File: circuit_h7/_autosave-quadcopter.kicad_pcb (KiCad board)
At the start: 4 copper layers, 37.5 x 37.5 mm, 128 parts, among them J1 Conn_01x01_Female, J10 Conn_01x01_Female, J11 Conn_01x04_Male, J13 Conn_01x01_Female, J14 Conn_01x01_Female, J15 Conn_01x01_Female, J16 Conn_01x01_Female, J17 Conn_01x01_Female, J18 USB_C_Receptacle_USB2.0, J19 Conn_01x08_Male, J2 Conn_01x01_Female, J20 Conn_01x01_Female, J21 Conn_01x01_Female, J22 Conn_01x01_Female, J23 Conn_01x01_Female, J24 Conn_01x01_Female, J25 Conn_01x01_Female, J26 Conn_01x01_Female, J27 Conn_01x01_Female, J28 Conn_01x01_Female, J29 Conn_01x01_Female, J3 Conn_01x01_Female, J30 Conn_01x01_Female, J31 Conn_01x01_Female, J32 Conn_01x01_Female, J33 Conn_01x01_Female, J34 Conn_01x01_Female, J35 Conn_01x01_Female, J36 Conn_01x01_Female, J37 Conn_01x01_Female, J4 Conn_01x01_Female, J40 Conn_01x01_Female, J41 Conn_01x01_Female, J42 Conn_01x01_Female, J43 Conn_01x01_Female, J44 Conn_01x01_Female, J45 Conn_01x01_Female, J47 Conn_01x01_Female, J48 Conn_01x01_Female, J49 Conn_01x01_Female, J5 Conn_Coaxial, J50 Conn_01x01_Female, J6 Conn_01x06_Male, J7 Conn_01x01_Female, J8 Conn_01x01_Female, J9 Conn_01x01_Female, SW1 SW_DIP_x01, U1 STM32H723VGH6, U10 ESP8285, U12 TPS5430DDA, U2 ICM-42605, U3 DPS310, U4 3V3, U6 2450FM07D0034T, U7 W25Q80DVUXIE TR (16M), U8 SX1281, Y1 16M, Y2 52Mhz, 12pF, Y3 40M

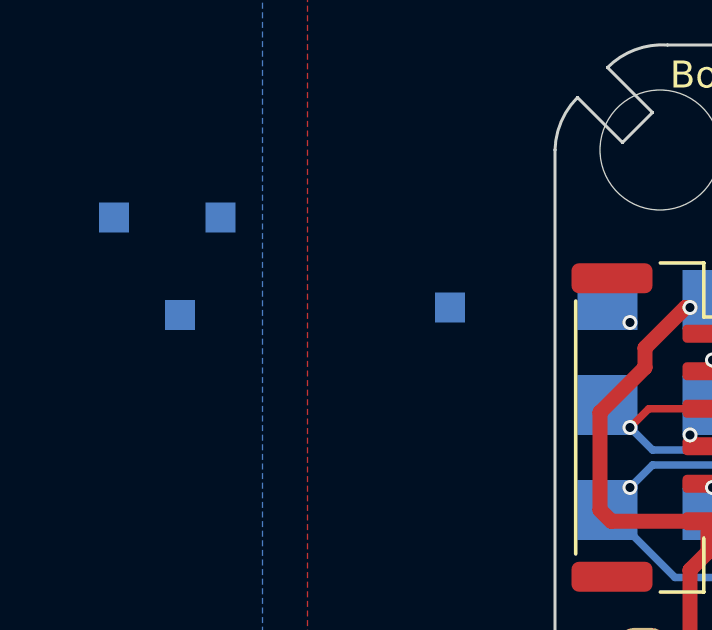
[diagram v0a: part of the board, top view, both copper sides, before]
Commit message: More work on H7 board. Removed ctrl mix from firmware
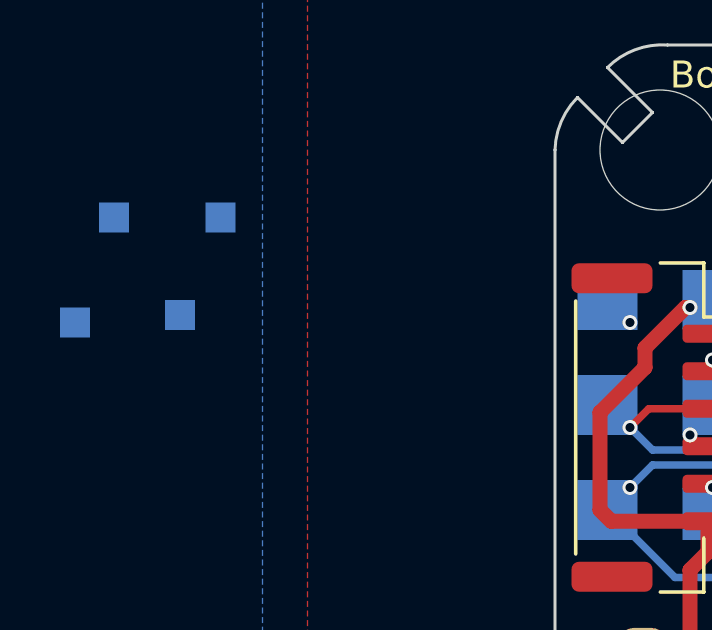
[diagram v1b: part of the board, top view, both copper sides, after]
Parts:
- moved J27 12.5 mm to (102.2, 78.0)
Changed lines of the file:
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@@
   )
   (footprint "TestPoint:TestPoint_Pad_1.0x1.0mm" (layer "B.Cu")
-    (at 114.75 77.5 180)
+    (at 102.25 78 180)
     (descr "SMD rectangular pad as test Point, square 1.0mm side length")
     (tags "test point SMD pad rectangle square")

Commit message: More work on H7 board
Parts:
- removed C42: 150p, Capacitor_SMD:C_0402_1005Metric
- removed C43: 100n, Capacitor_SMD:C_0402_1005Metric
- removed C44: 1.5n, Capacitor_SMD:C_0402_1005Metric
- removed C45, C46: 10u, Capacitor_SMD:C_0805_2012Metric
- removed R17: 300, Resistor_SMD:R_0402_1005Metric
- removed R19: 10k, Resistor_SMD:R_0402_1005Metric
- added C14: 22uF 25v, Capacitor_SMD:C_0805_2012Metric, F.Cu at (132.2, 99.5)
- added C15: 22n, Capacitor_SMD:C_0402_1005Metric, F.Cu at (128.0, 97.2)
- added C20: 100uF 6.3V, Capacitor_SMD:C_1206_3216Metric, F.Cu at (136.0, 94.0)
- added L2: 10u 2A, Inductor_SMD:L_Taiyo-Yuden_MD-4040, F.Cu at (131.2, 95.5)
- added R7: 10k, Resistor_SMD:R_0402_1005Metric, F.Cu at (150.5, 97.8)
- added R8: 100k, Resistor_SMD:R_0402_1005Metric, F.Cu at (124.8, 99.5)
- added U5: MT2492 600kHz 16v 2A, Package_TO_SOT_SMD:SOT-23-6, F.Cu at (129.0, 99.5)
- R10: value 3.3K -> 1.4k
- R11: value 300 -> 13k; footprint Resistor_SMD:R_0402_1005Metric -> Resistor_SMD:R_0603_1608Metric
- U12: value TPS5430DDA -> TPS5430DDA 3A 36v
- moved J27 43.9 mm to (146.0, 81.0)
- moved J35 40.7 mm to (144.0, 79.0)
- moved J34 40.3 mm to (146.0, 79.0)
- moved J36 37.5 mm to (144.0, 81.0)
- moved R11 23.9 mm to (126.0, 99.8)
- moved F1 12.4 mm to (115.2, 94.0), turned to 180 degrees
- moved R10 1.06 mm to (150.5, 98.8)
- moved D1 0.50 mm to (126.0, 104.2)
- moved C40 0.25 mm to (132.2, 103.8)
- moved C41 0.25 mm to (128.8, 103.8)
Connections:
- net Net-(R9-Pad2) renamed /ELRS_LED
- D5 pad 2: unconnected-(D5-Pad2) -> Net-(C20-Pad1)
- R10 pad 2: Net-(C43-Pad2) -> Net-(R10-Pad2)
- R11 pad 2: Net-(C42-Pad1) -> Net-(R8-Pad1)
- U12 pad 4: Net-(C42-Pad1) -> Net-(R10-Pad2)
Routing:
- net Net-(C20-Pad1): track 0.00 -> 15.9 mm, vias 0 -> 2
- net /ELRS_LED: track 11.3 -> 24.0 mm, vias 2 -> 3
- net /UART1_RX: track 55.6 -> 44.4 mm, vias 6 -> 4
- net Net-(C42-Pad1): track 10.8 -> 0.00 mm
- net Net-(R10-Pad2): track 0.00 -> 8.21 mm
- net /IMU_pwr: track 26.0 -> 19.1 mm
- net /USB_DP: track 24.0 -> 18.7 mm
- net Net-(L2-Pad1): track 0.00 -> 4.96 mm
- net +10V: track 63.1 -> 58.3 mm
- net /USB_DN: track 23.8 -> 19.6 mm
- net Net-(R8-Pad1): track 0.00 -> 3.46 mm
- net GND: track 47.6 -> 49.7 mm
- net /BATT_DIV: track 11.4 -> 9.43 mm
- net Net-(D1-Pad2): track 1.51 -> 0.00 mm
- net Net-(C15-Pad1): track 0.00 -> 1.44 mm
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
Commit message: Started to revamp gyro and imu interp with att platform to fix errors and be consistent. Moved some code out of IMU drivers to imu_shared, or delted
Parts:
- added J38: Conn_01x01_Female, TestPoint:TestPoint_Pad_1.0x1.0mm, B.Cu at (147.5, 77.5)
- moved J34 2.83 mm to (144.0, 81.0)
- moved J27 2.00 mm to (146.0, 79.0)
- moved J36 2.00 mm to (146.0, 81.0)
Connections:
- U10 pad 15: unconnected-(U10-Pad15) -> /ELRS_BOOT
- U5 pad 1: Net-(C15-Pad1) -> +10V
- U5 pad 2: GND -> unconnected-(U5-Pad2)
- U5 pad 3: Net-(R8-Pad1) -> +10V
- U5 pad 4: +10V -> Net-(R8-Pad1)
- U5 pad 5: +10V -> Net-(C15-Pad1)
- U5 pad 6: Net-(L2-Pad1) -> unconnected-(U5-Pad6)
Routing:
- net /TX_ELRS: track 15.9 -> 15.1 mm
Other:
- board text added: "B"
- board text added: "C"
- board text added: "D"
- board text added: "R"
- board text added: "T"
